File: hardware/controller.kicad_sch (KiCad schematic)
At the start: 82 parts, among them J1 USB_B_Micro, J10 Conn_01x06 Header, J11 Conn_01x04 MiniPV, J16 Conn_01x03 MiniPV, J17 Conn_01x03 MiniPV, J2 Conn_01x04 Header, J3 Conn_01x02 MiniPV, J4 Conn_01x02 MiniPV, J5 Conn_01x03 MiniPV, J6 Conn_01x03 MiniPV, J7 Conn_01x03 MiniPV, J8 Conn_01x03 MiniPV, J9 Conn_01x03 MiniPV, Q1 AO3400A, Q2 AO3400A, Q3 AO3400A, Q4 AO3400A, Q7 AO3400A, SW1 SW_Push, U1 STM32G030C8T6, U2 CH340C, U3 MAX31855KASA, U4 MAX31855KASA

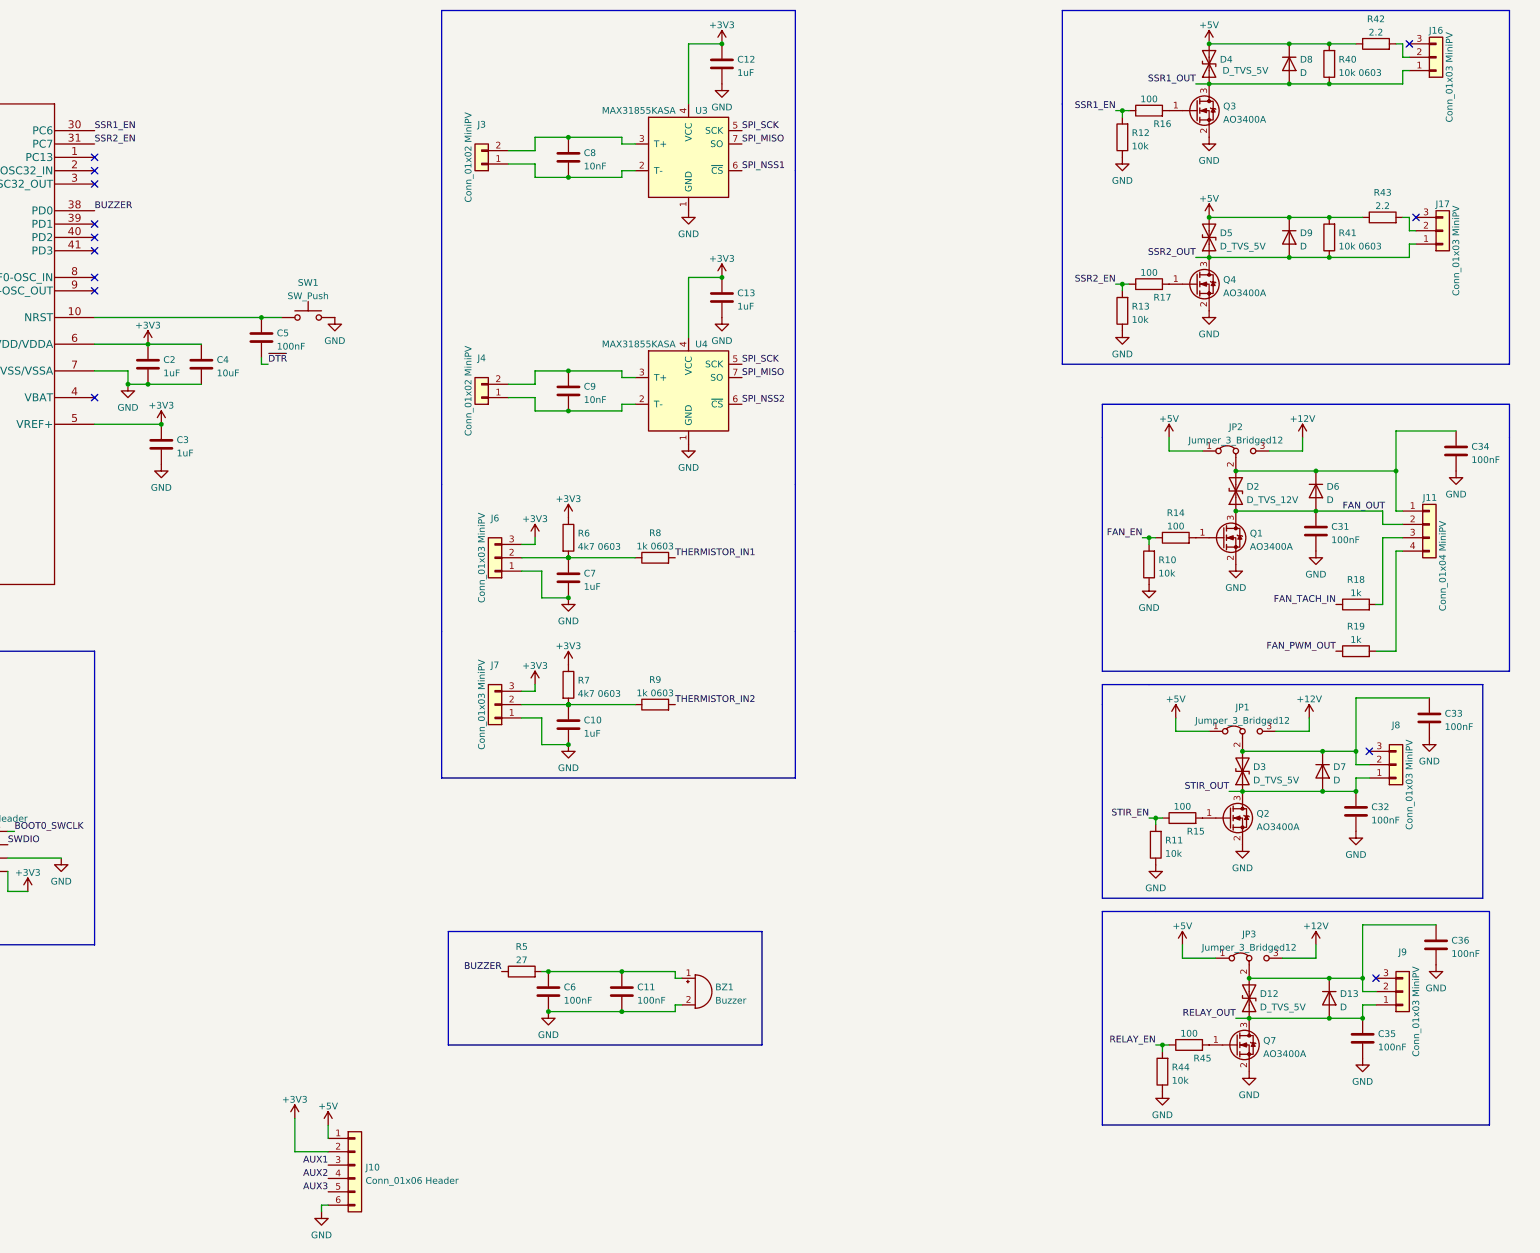
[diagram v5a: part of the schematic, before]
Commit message: Add internal thermistor and change SSR2 -> mosfet
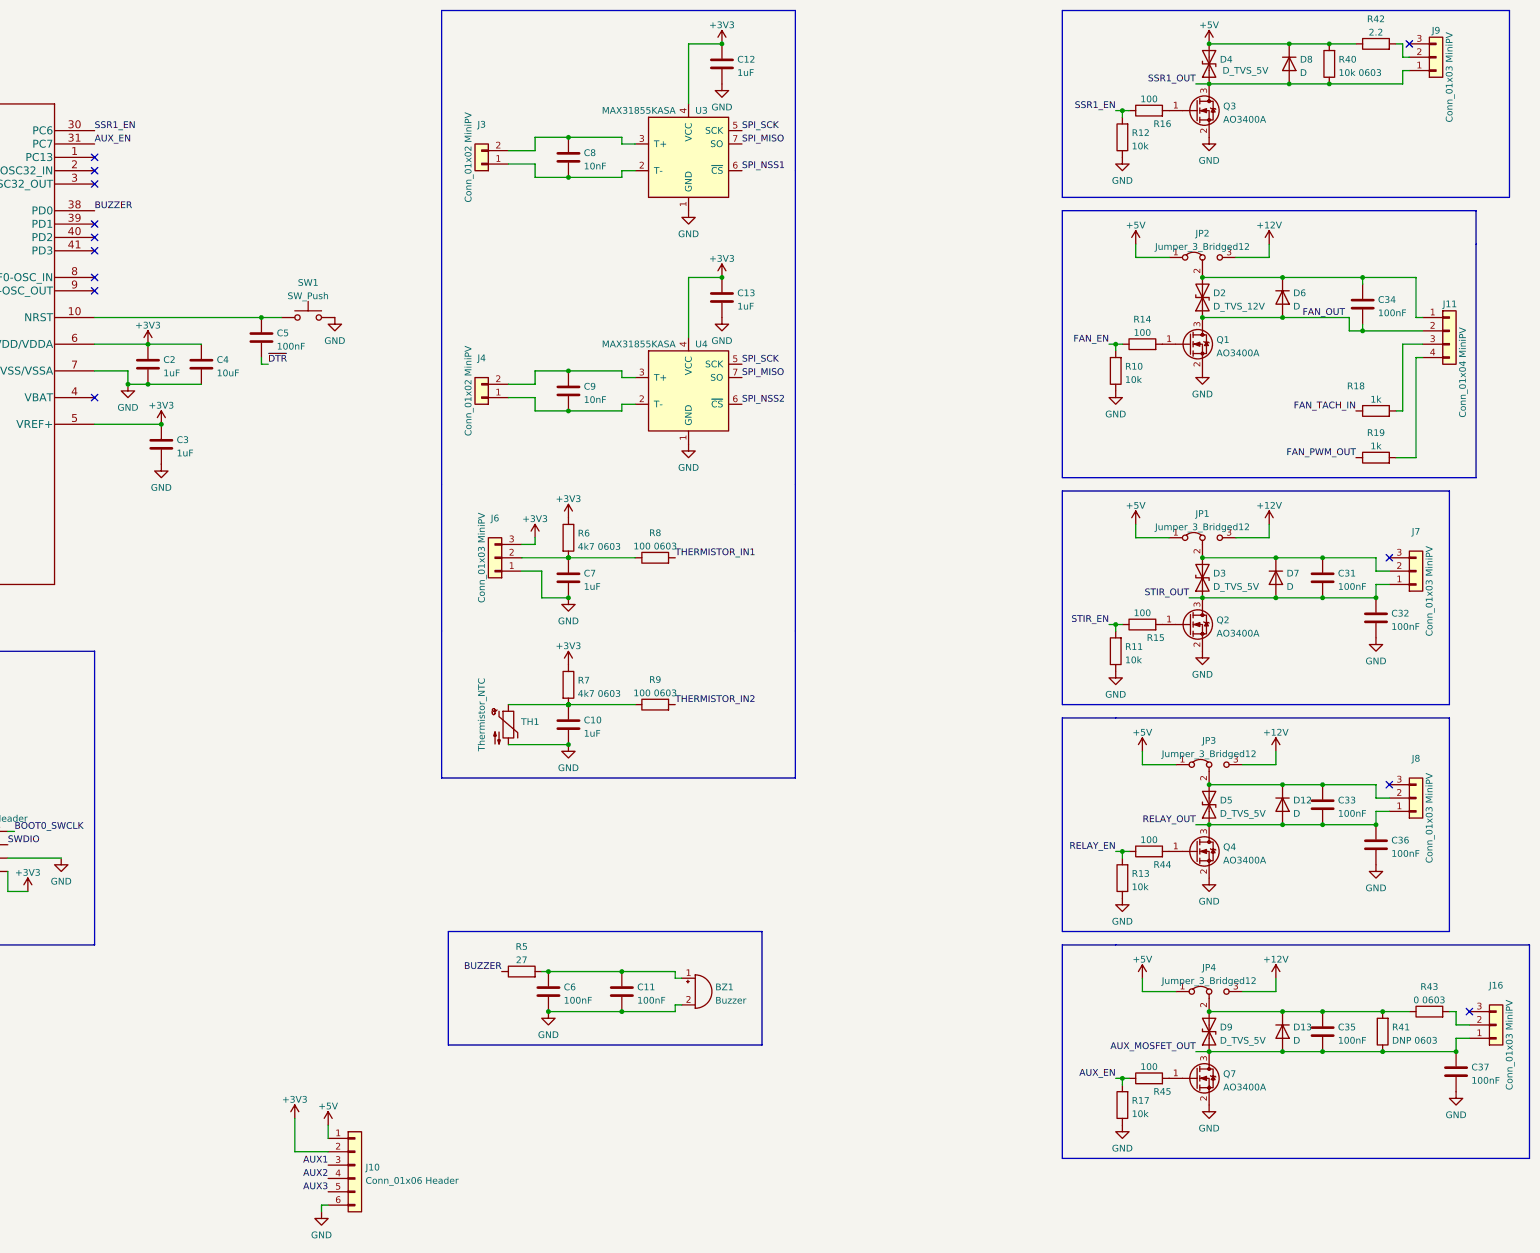
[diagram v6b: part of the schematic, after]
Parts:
- removed C36: 100nF, Capacitor_SMD:C_0402_1005Metric, symbol Device:C
- removed D5: D_TVS_5V, Diode_SMD:D_SMA_Handsoldering, symbol Device:D_TVS
- removed D9: D, Diode_SMD:D_SMA, symbol Device:D
- removed J17, J7: Conn_01x03 MiniPV, Homebrew:MiniPV_69167-X03XXX_1x03_P2.54mm_Polarized_Vertical, symbol Connector_Generic:Conn_01x03
- removed Q4: AO3400A, Package_TO_SOT_SMD:SOT-23, symbol Transistor_FET:AO3400A
- removed R13: 10k, Resistor_SMD:R_0402_1005Metric, symbol Device:R
- added C35, C37: 100nF, Capacitor_SMD:C_0402_1005Metric, symbol Device:C
- added D13: D, Diode_THT:D_DO-201AD_P12.70mm_Horizontal, symbol Device:D
- added D9: D_TVS_5V, Diode_SMD:D_SMA_Handsoldering, symbol Device:D_TVS
- added J16: Conn_01x03 MiniPV, Homebrew:MiniPV_69167-X03XXX_1x03_P2.54mm_Polarized_Vertical, symbol Connector_Generic:Conn_01x03
- added JP4: Jumper_3_Bridged12, Connector_PinHeader_2.54mm:PinHeader_1x03_P2.54mm_Vertical, symbol Jumper:Jumper_3_Bridged12
- added Q7: AO3400A, Package_TO_SOT_SMD:SOT-23, symbol Transistor_FET:AO3400A
- added R45: 100, Resistor_SMD:R_0402_1005Metric, symbol Device:R
- added TH1: Thermistor_NTC, Capacitor_THT:C_Disc_D3.0mm_W2.0mm_P2.50mm, symbol Device:Thermistor_NTC
- D12: renamed from D13; footprint Diode_SMD:D_SMA -> Diode_THT:D_DO-201AD_P12.70mm_Horizontal; LCSC C8678 -> (none); MPN (none) -> SB10150TA
- D6, D7, D8: footprint Diode_SMD:D_SMA -> Diode_THT:D_DO-201AD_P12.70mm_Horizontal; LCSC C8678 -> (none); MPN (none) -> SB10150TA
- R17: value 100 -> 10k; LCSC C25076 -> C25744
- R41: value 10k 0603 -> DNP 0603
- R43: value 2.2 -> 0 0603
- R8, R9: value 1k 0603 -> 100 0603; LCSC C21190 -> C22775
- renumbered C35 to C36, D12 to D5, J8 to J7, J9 to J8, J16 to J9, Q7 to Q4, R44 to R13, R45 to R44
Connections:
- net +12V: now also JP4.3 (B)
- net +5V: now also JP4.1 (A); no longer R41.2, R43.1
- net FAN_OUT: now also C34.2; no longer C31.1
- net GND: now also R17.1, C37.2, Q7.2 (S), TH1.2; no longer C31.2, C33.2, C34.2
- net RELAY_OUT: now also C33.2
- net STIR_OUT: now also C31.2
- net at D3.2 (A2), D7.1 (K), J7.2 (Pin_2)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: now also C31.1; no longer C33.1
- net at C10.1, R7.2, R9.1: now also TH1.1
- net at R43.2: now also J16.2 (Pin_2)
- net at D12.1 (K), D5.2 (A2), J8.2 (Pin_2)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: now also C33.1
- net AUX_EN: now reaches R17.2
- net AUX_EN: now also U1.31 (PC7), R45.1
- removed net SSR2_EN: R17.1, U1.31 (PC7)
- net SSR2_OUT renamed AUX_MOSFET_OUT
- net AUX_MOSFET_OUT: now also C35.2, C37.1, D13.2 (A), D9.1 (A1), J16.1 (Pin_1), Q7.3 (D)
- new net: C35.1, D13.1 (K), D9.2 (A2), JP4.2 (C), R41.2, R43.1
- new net: Q7.1 (G), R45.2
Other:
- moved on the sheet: C32, C34, C36, D12, D2, D3, D5, D6, D7, J11, J7, J8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

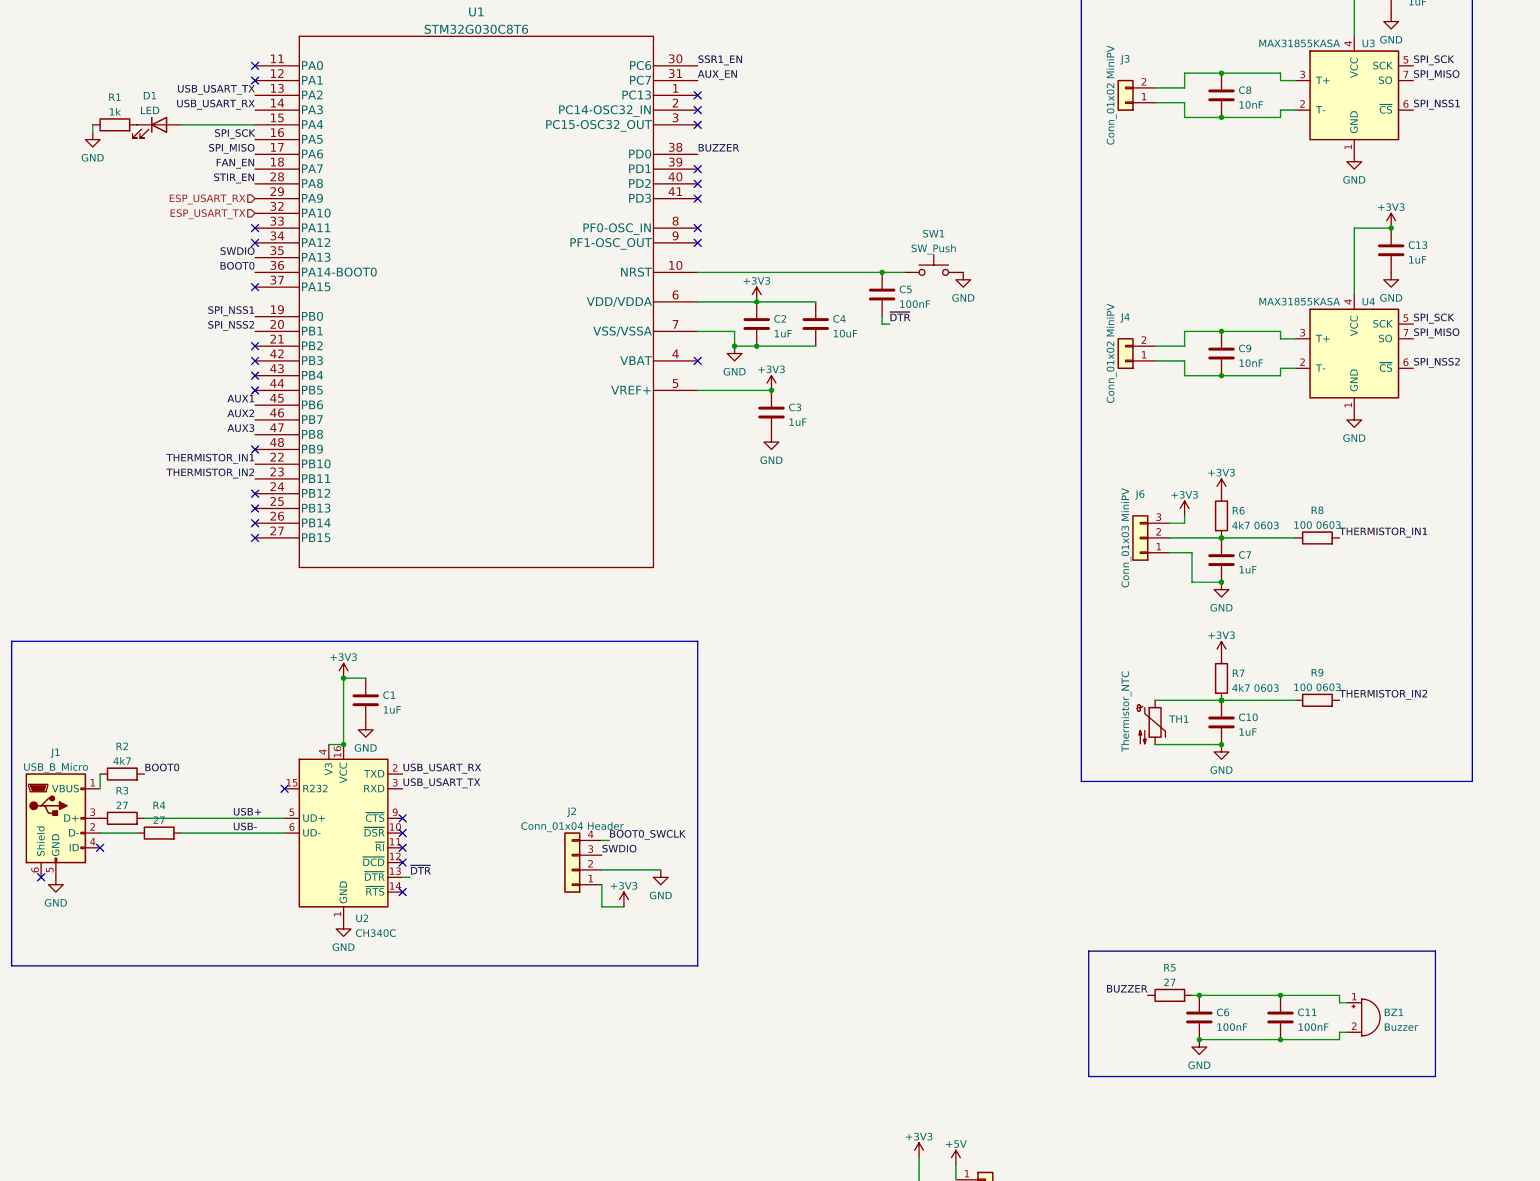
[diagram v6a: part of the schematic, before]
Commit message: Continue layout, add SPI flash
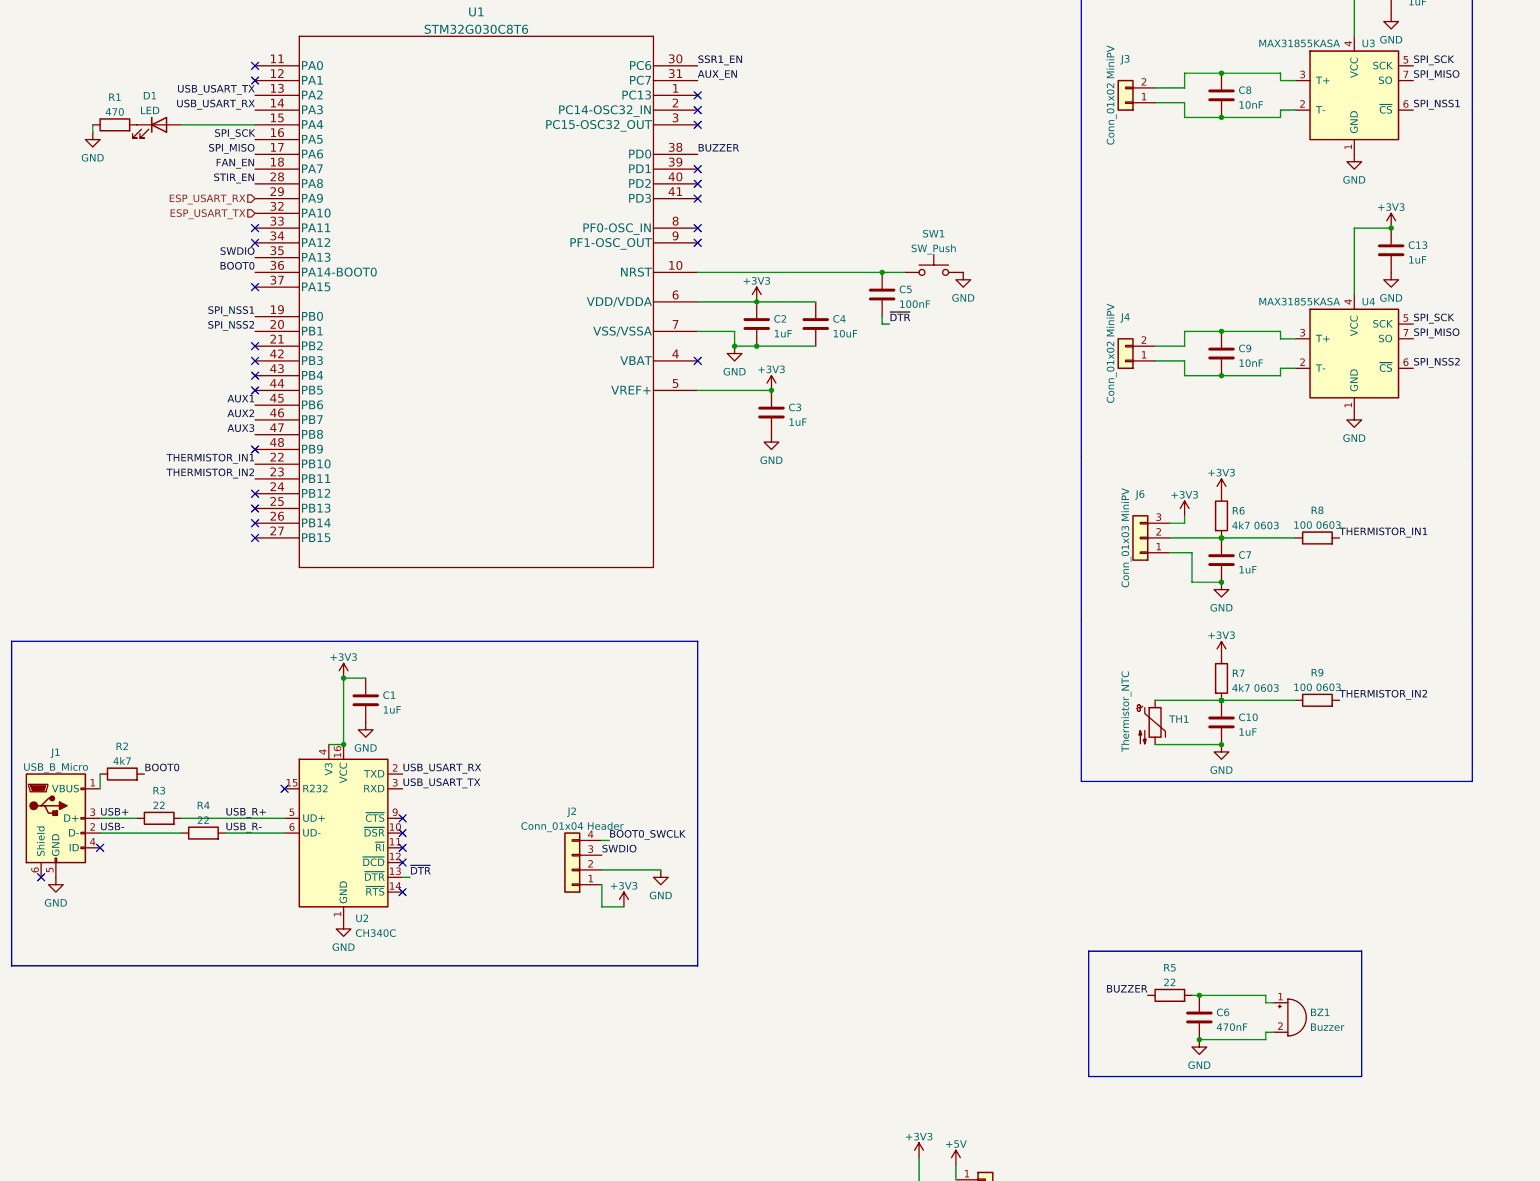
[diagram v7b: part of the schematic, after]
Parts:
- removed C11: 100nF, Capacitor_SMD:C_0402_1005Metric, symbol Device:C
- C6: value 100nF -> 470nF; LCSC C307331 -> C47339
- D12, D13, D6, D7, D8: footprint Diode_THT:D_DO-201AD_P12.70mm_Horizontal -> Diode_SMD:D_SMA; LCSC (none) -> C8678; MPN SB10150TA -> (none)
- R1: value 1k -> 470; LCSC C11702 -> C25117
- R3, R4, R5: value 27 -> 22; footprint Resistor_SMD:R_0603_1608Metric -> Resistor_SMD:R_0402_1005Metric; LCSC C25190 -> C25091
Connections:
- net USB+: now also J1.3 (D+), R3.1; no longer R3.2, U2.5 (UD+)
- net USB-: now also J1.2 (D-), R4.1; no longer R4.2, U2.6 (UD-)
- new net USB_R+: R3.2, U2.5 (UD+)
- new net USB_R-: R4.2, U2.6 (UD-)
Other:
- moved on the sheet: BZ1, R3, R4

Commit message: Continue layout
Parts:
- removed C1: 1uF, Capacitor_SMD:C_0402_1005Metric, symbol Device:C
- removed C5: 100nF, Capacitor_SMD:C_0402_1005Metric, symbol Device:C
- removed J1: USB_B_Micro, Homebrew:FRAMATOME_10118194-0001LF_fixed_bridges, symbol Connector:USB_B_Micro
- removed R4: 22, Resistor_SMD:R_0402_1005Metric, symbol Device:R
- removed U2: CH340C, Package_SO:SOIC-16_3.9x9.9mm_P1.27mm, symbol Interface_USB:CH340C
- added SW4: SW_Push, Homebrew:SW_TACTILE_5.1MM_TS-1187A-C-D-B, symbol Switch:SW_Push
- R2: value 4k7 -> 10k; LCSC C25900 -> C25744
- R3: value 22 -> 100k; LCSC C25091 -> C25741
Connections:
- net BOOT0_SWCLK is gone; now on net SWCLK: J2.4 (Pin_4)
- net USB+ is gone; now on net GND: R3.1
- net USB_R+ is gone; now on net SWCLK: R3.2
- net +3V3: now also R2.2
- net at R2.1: now also SW4.1
- net BOOT0 renamed SWCLK
- net SWCLK: now also SW4.2; no longer R2.2
- net USB_USART_RX: no longer names the net of U1.14 (PA3)
- net USB_USART_TX: no longer names the net of U1.13 (PA2)
- no-connect marks 36 -> 30
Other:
- moved on the sheet: SW1
